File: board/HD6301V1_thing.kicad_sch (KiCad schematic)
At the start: 14 parts, among them SW1 Reset, U1 74HC00, U2 HD6301V1, U3 AS7C256B, U4 28C256, X1 CXO_DIP14

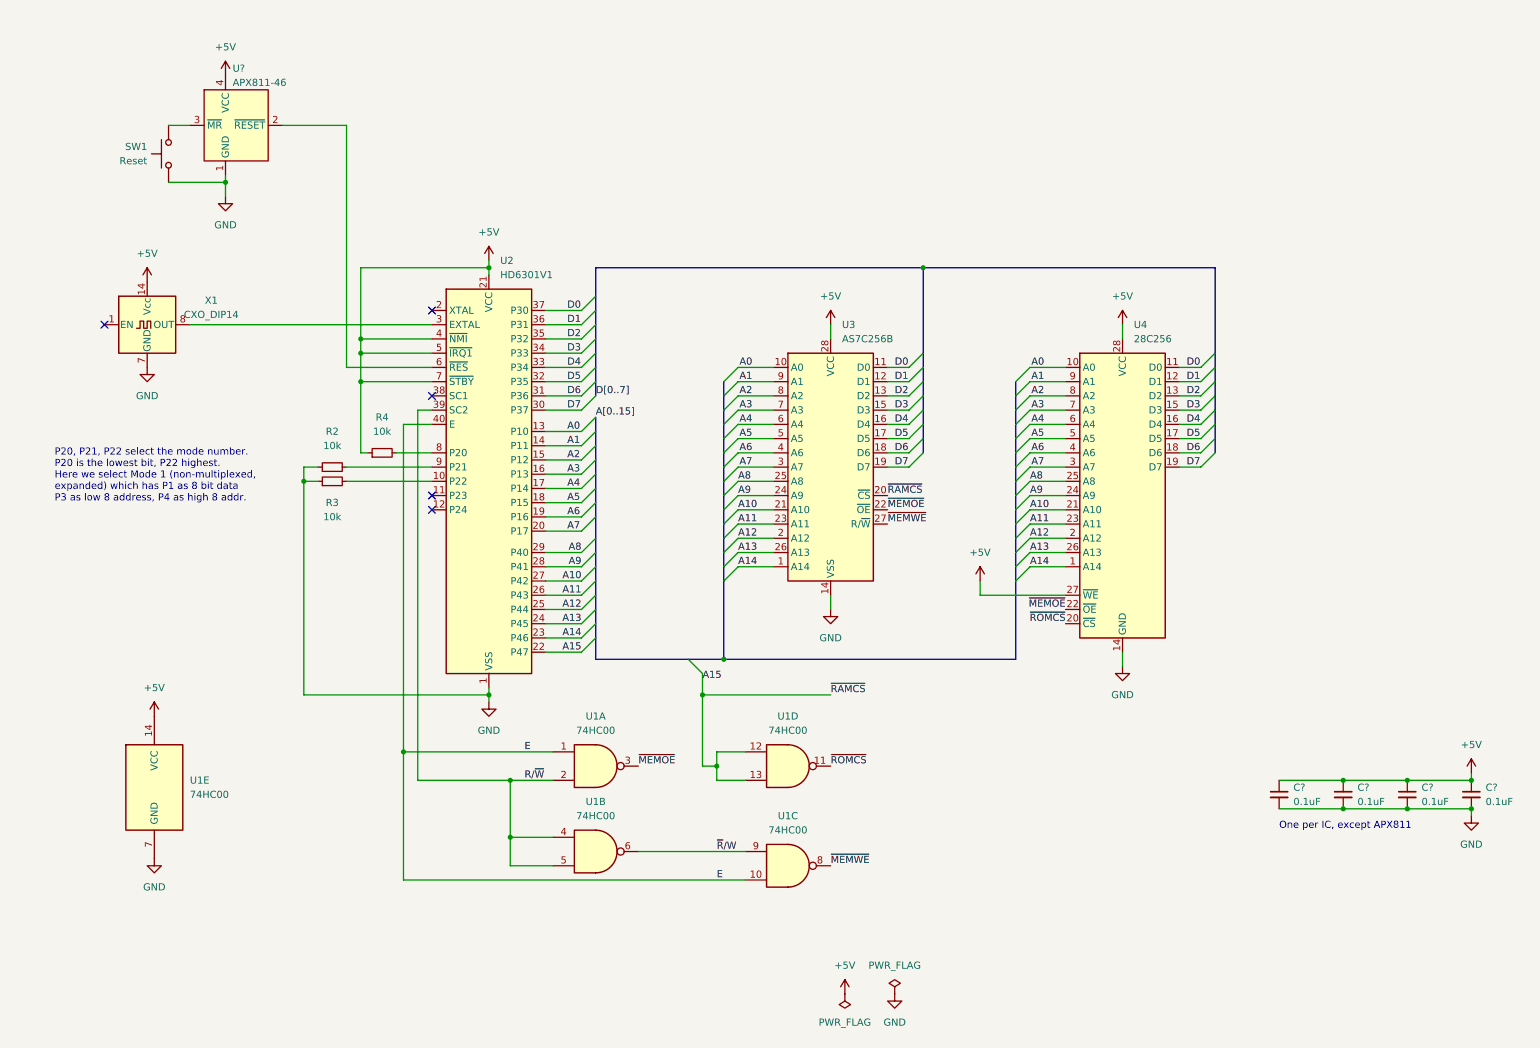
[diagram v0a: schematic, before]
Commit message: Update the schematic to use mode 2 and multiplexed P3
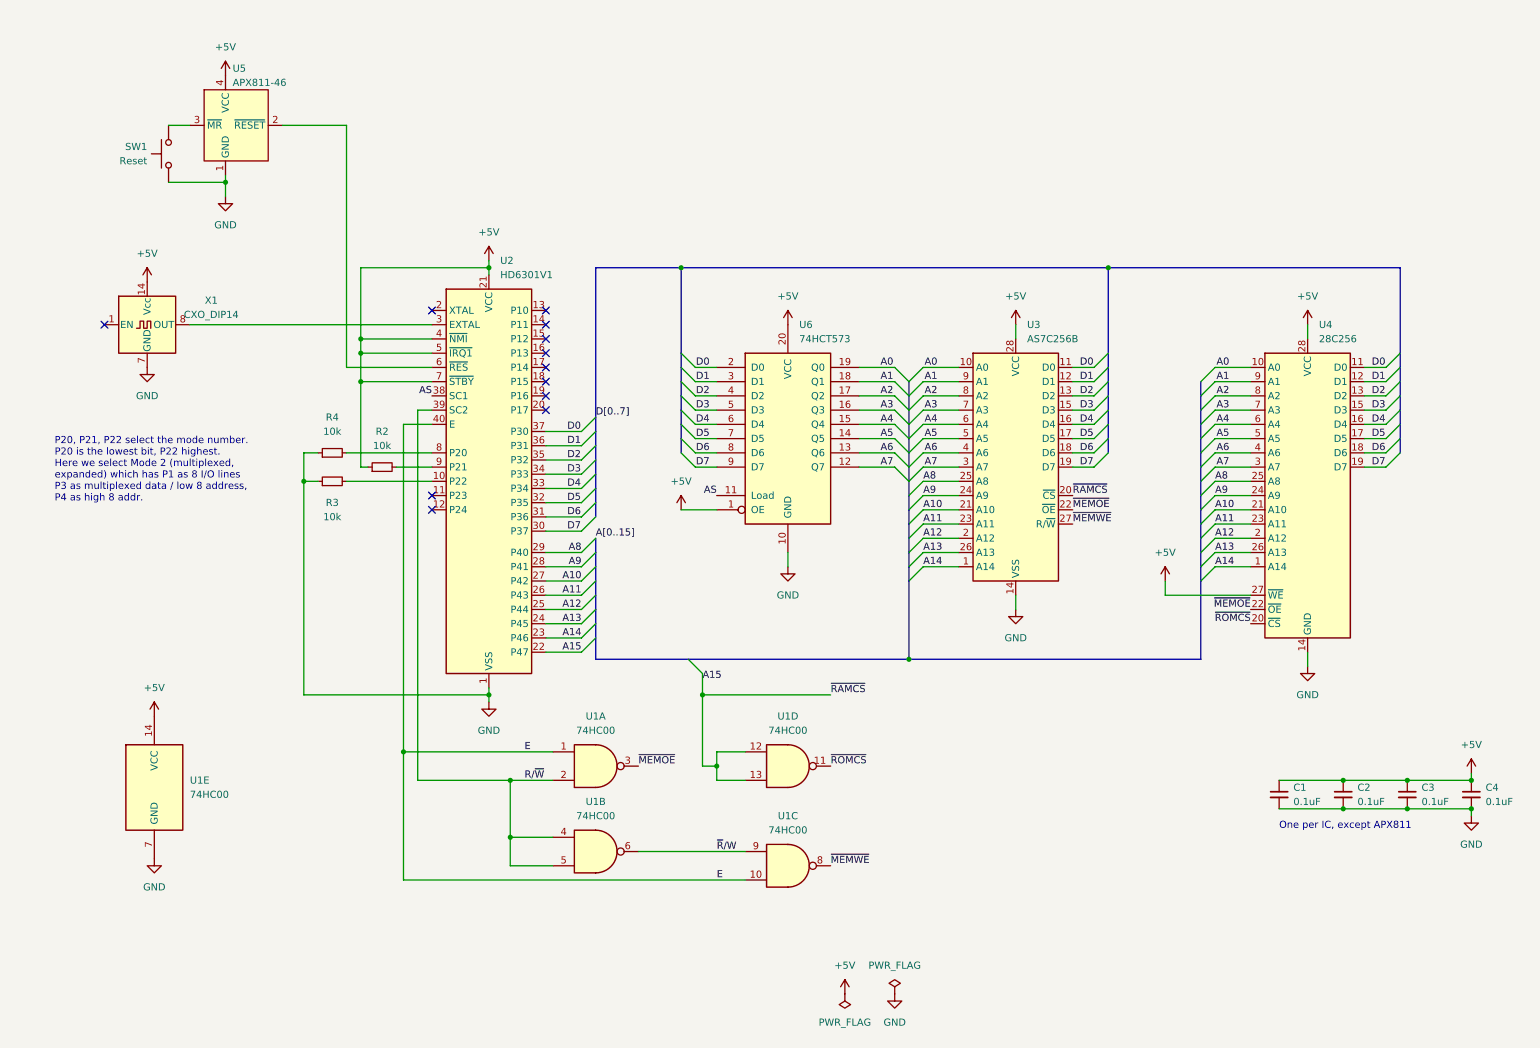
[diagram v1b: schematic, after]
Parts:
- added U6: 74HCT573, symbol 74xx:74LS573
- gave numbers to parts that had none: 5
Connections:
- net +5V: now also R2.1, U6.1 (OE), U6.20 (VCC); no longer R4.1
- net A0: now also U6.19 (Q0); no longer U2.13 (P10)
- net A1: now also U6.18 (Q1); no longer U2.14 (P11)
- net A2: now also U6.17 (Q2); no longer U2.15 (P12)
- net A3: now also U6.16 (Q3); no longer U2.16 (P13)
- net A4: now also U6.15 (Q4); no longer U2.17 (P14)
- net A5: now also U6.14 (Q5); no longer U2.18 (P15)
- net A6: now also U6.13 (Q6); no longer U2.19 (P16)
- net A7: now also U6.12 (Q7); no longer U2.20 (P17)
- net D0: now also U6.2 (D0)
- net D1: now also U6.3 (D1)
- net D2: now also U6.4 (D2)
- net D3: now also U6.5 (D3)
- net D4: now also U6.6 (D4)
- net D5: now also U6.7 (D5)
- net D6: now also U6.8 (D6)
- net D7: now also U6.9 (D7)
- net GND: now also R4.1, U6.10 (GND); no longer R2.1
- net AS: now reaches U2.38 (SC1)
- net AS: now also U6.11 (Load)
- no-connect marks 5 -> 12
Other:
- note added: "P20, P21, P22 select the mode number. P20 is the lowest bit, P22 highest. Here we select Mode 2 (multiplexed, expanded) which has P1 as 8 I/O lines P3 as multiplexed data / low 8 address, P4 as high 8 addr."
- note removed: "P20, P21, P22 select the mode number. P20 is the lowest bit, P22 highest. Here we select Mode 1 (non-multiplexed, expanded) which has P1 as 8 bit data P3 as low 8 address, P4 as high 8 addr."
- moved on the sheet: R2, R4, U3, U4

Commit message: Add USB and P2.0-P2.2 setup
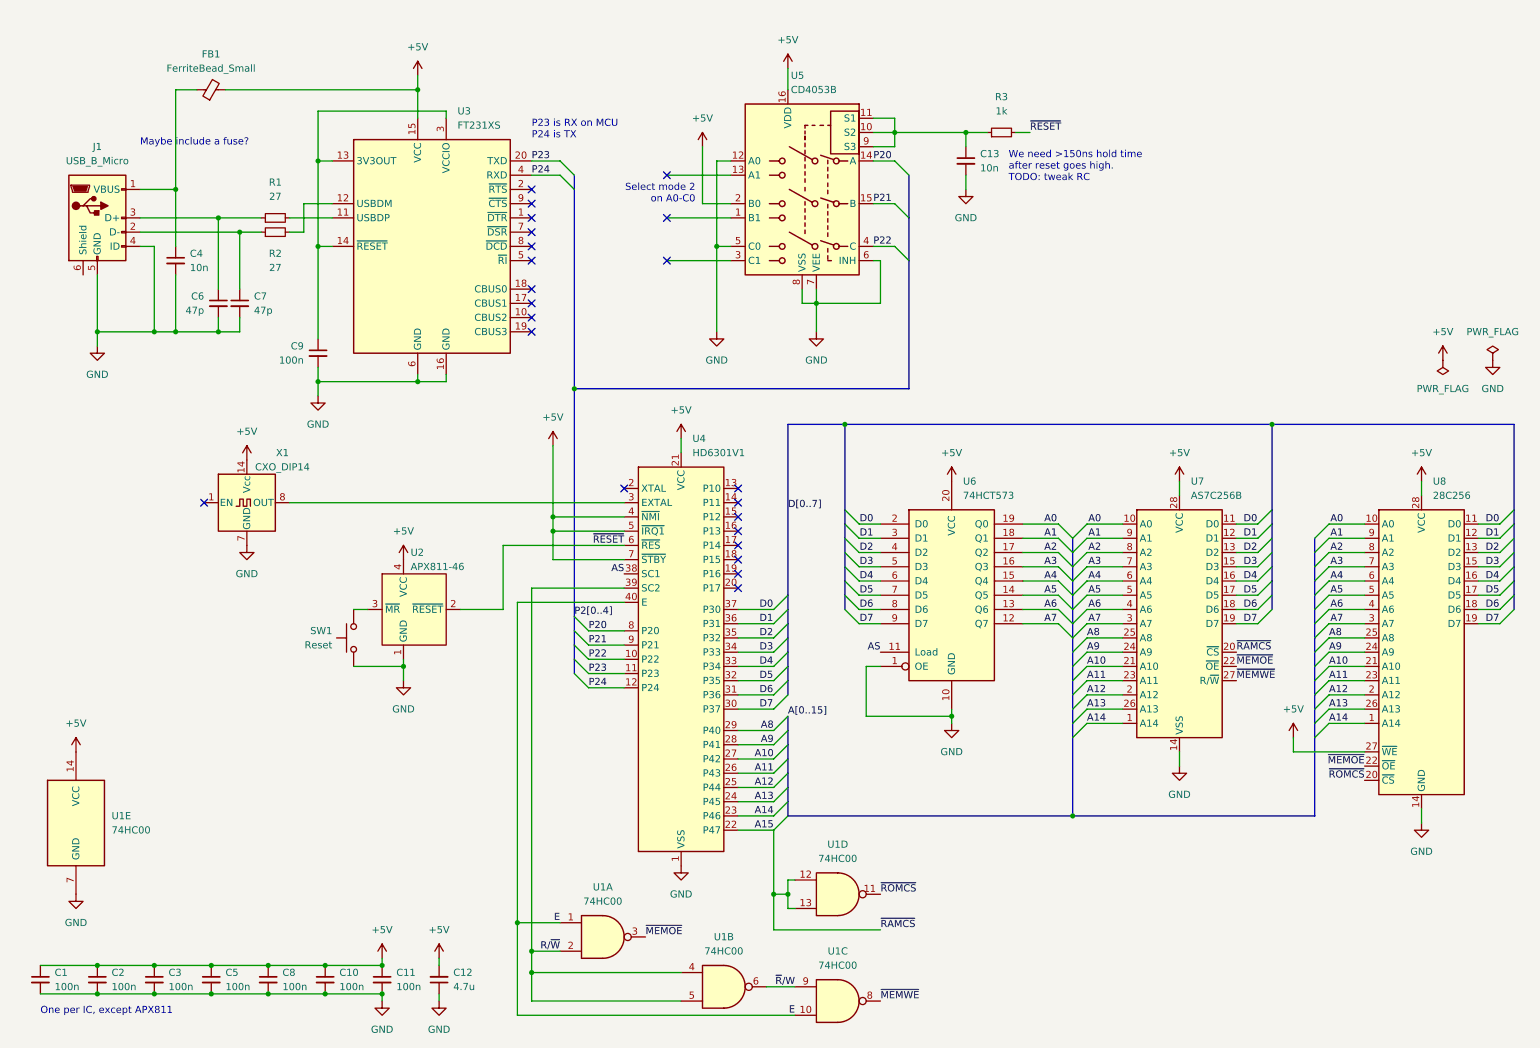
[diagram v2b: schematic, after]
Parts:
- removed R4: 10k, symbol Device:R_Small
- added C1, C2, C3, C9: 100n, symbol Device:C_Small
- added C12: 4.7u, symbol Device:C_Small
- added C13, C4: 10n, symbol Device:C_Small
- added C6, C7: 47p, symbol Device:C_Small
- added FB1: FerriteBead_Small, symbol Device:FerriteBead_Small
- added J1: USB_B_Micro, symbol Connector:USB_B_Micro
- added R1: 27, symbol Device:R_Small
- added U3: FT231XS, Package_SO:SSOP-20_3.9x8.7mm_P0.635mm, symbol Interface_USB:FT231XS
- added U5: CD4053B, symbol Analog_Switch:CD4053B
- C10: renamed from C3; value 0.1uF -> 100n
- C11: renamed from C4; value 0.1uF -> 100n
- C5: renamed from C1; value 0.1uF -> 100n
- C8: renamed from C2; value 0.1uF -> 100n
- R2: value 10k -> 27
- R3: value 10k -> 1k
- renumbered U5 to U2, U2 to U4, U3 to U7, U4 to U8
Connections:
- net +5V: now also C1.1, C12.2, C2.1, C3.1, FB1.2, U3.15 (VCC), U5.16 (VDD), U5.2 (B0); no longer R2.1, U6.1 (OE)
- net GND: now also U6.1 (OE), C1.2, C12.1, C13.2, C2.2, C3.2, C4.2, C6.2, C7.2, C9.2, J1.4 (ID), J1.5 (GND), U3.16 (GND), U3.6 (GND), U5.12 (A0), U5.5 (C0), U5.6 (INH), U5.7 (VEE), U5.8 (VSS); no longer R3.1
- net at R2.2: now also U3.12 (USBDM); no longer U4.9 (P21)
- net ~{RESET}: now reaches U2.2 (~{RESET}), U4.6 (~{RES})
- net ~{RESET}: now also R3.2
- net P20: now reaches U4.8 (P20)
- net P20: now also U5.14 (A)
- net P22: now reaches U4.10 (P22)
- net P22: now also U5.4 (C); no longer R3.2
- net P23: now reaches U4.11 (P23)
- net P23: now also U3.20 (TXD)
- net P24: now reaches U4.12 (P24)
- net P24: now also U3.4 (RXD)
- new net: C13.1, R3.1, U5.10 (S2), U5.11 (S1), U5.9 (S3)
- new net: R1.2, U3.11 (USBDP)
- new net: C9.1, U3.13 (3V3OUT), U3.14 (~{RESET}), U3.3 (VCCIO)
- new net: C7.1, J1.2 (D-), R2.1
- new net: C4.1, FB1.1, J1.1 (VBUS)
- new net: C6.1, J1.3 (D+), R1.1
- new net P21: U4.9 (P21), U5.15 (B)
- no-connect marks 12 -> 23
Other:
- note added: "Maybe include a fuse?"
- note added: "P23 is RX on MCU P24 is TX"
- note added: "Select mode 2 on A0-C0"
- note added: "We need >150ns hold time after reset goes high. TODO: tweak RC"
- note removed: "P20, P21, P22 select the mode number. P20 is the lowest bit, P22 highest. Here we select Mode 2 (multiplexed, expanded) which has P1 as 8 I/O lines P3 as multiplexed data / low 8 address, P4 as high 8 addr."
- moved on the sheet: C10, C11, C5, C8, SW1, U1A, U1B, U1C, U1D, U1E, U2, U4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
